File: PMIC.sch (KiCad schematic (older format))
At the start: 37 parts, among them J6 USB_B_Micro, U4 STPMIC1APQR

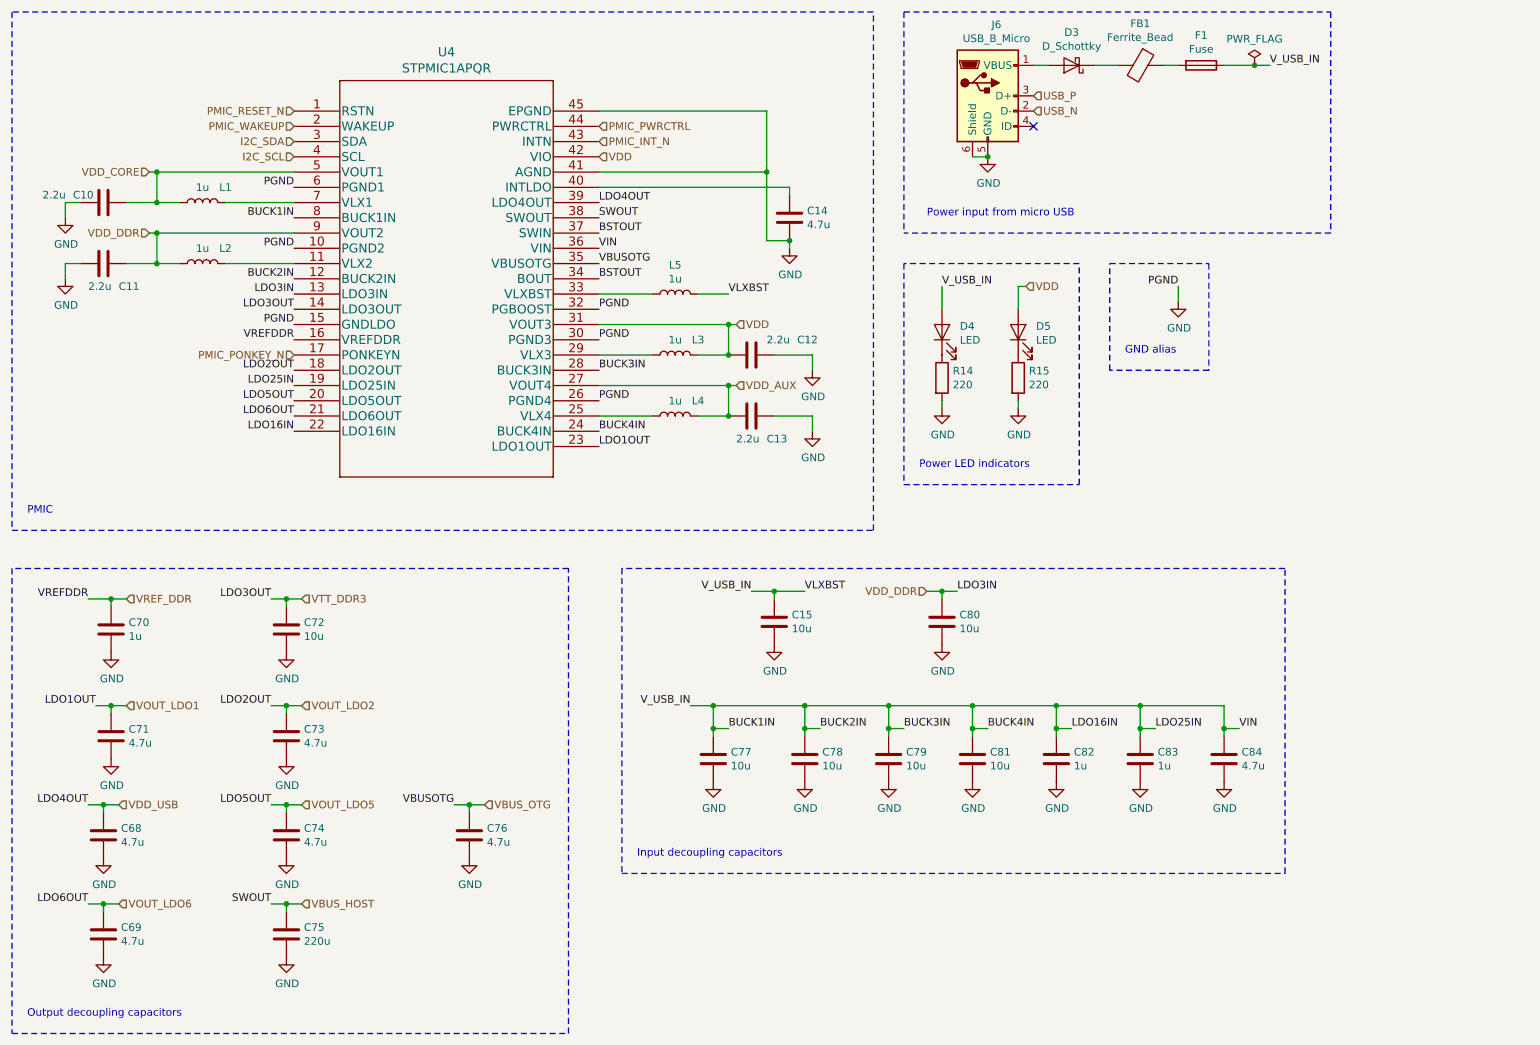
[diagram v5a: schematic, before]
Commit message: Add DC barrel connector for alternate power supply
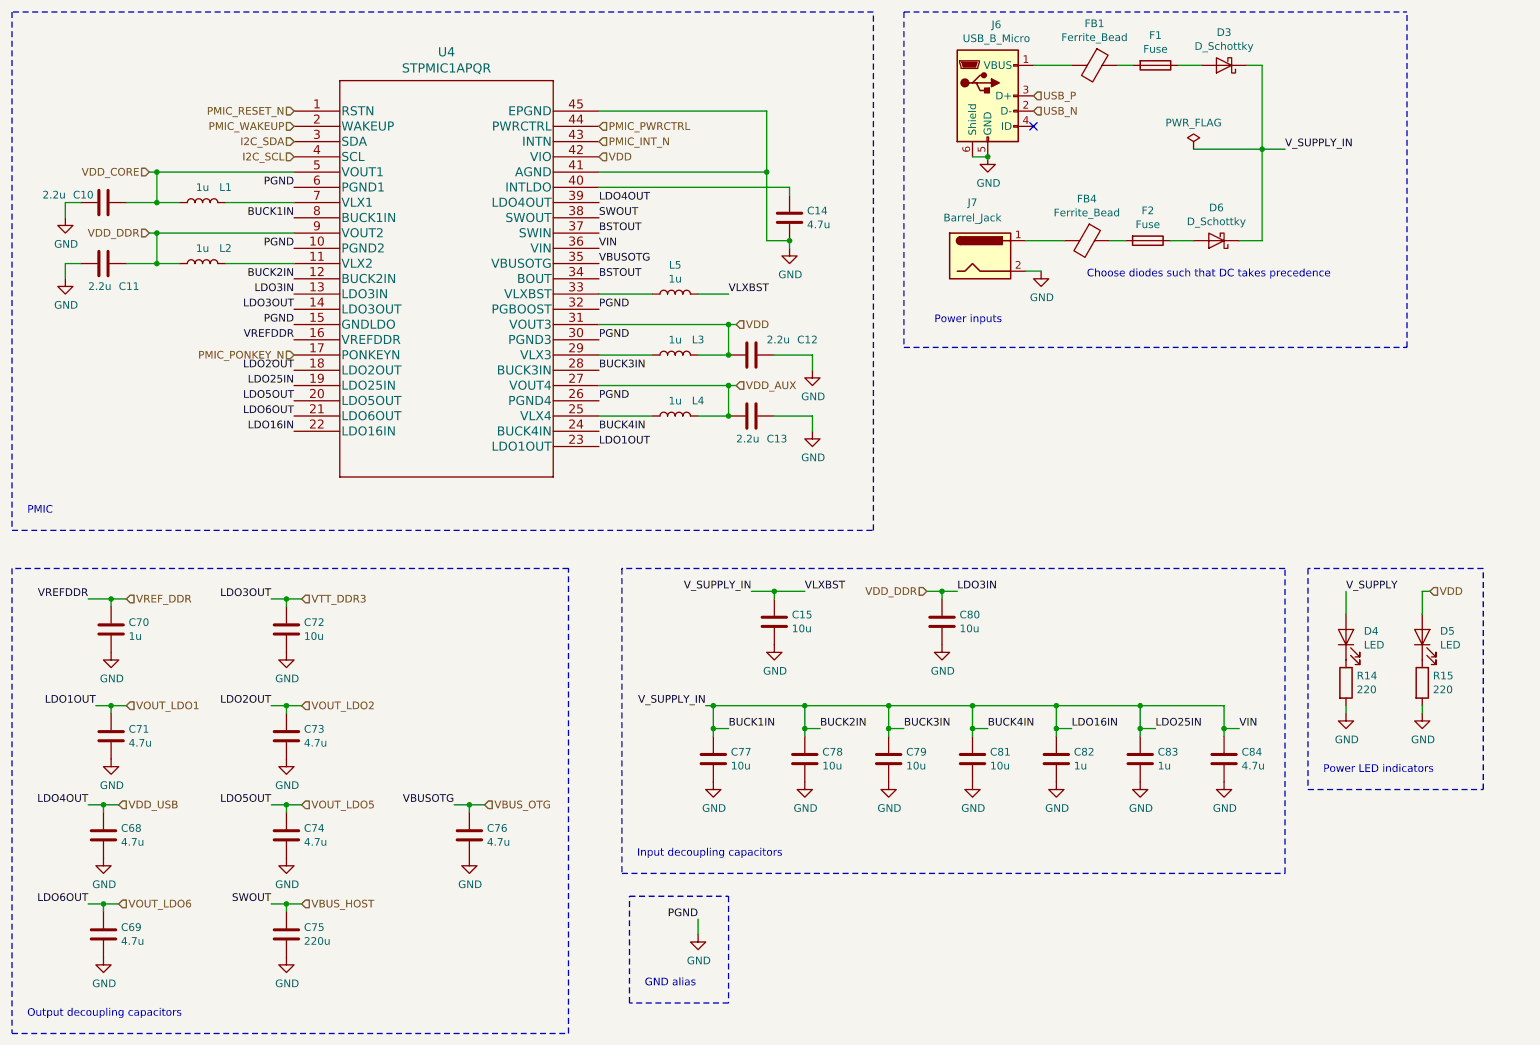
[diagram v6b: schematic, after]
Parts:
- added D6: D_Schottky, Diode_SMD:D_0603_1608Metric, symbol Device:D_Schottky
- added F2: Fuse, Fuse:Fuse_0603_1608Metric, symbol Device:Fuse
- added FB4: Ferrite_Bead, Inductor_SMD:L_0603_1608Metric, symbol Device:Ferrite_Bead
- added J7: Barrel_Jack, symbol Connector:Barrel_Jack
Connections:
- net BUCK1IN: now also D3.1 (K), D6.1 (K); no longer D4.2 (A), F1.1
- net GND: now also J7.2
- net at J6.1 (VBUS): now also FB1.2; no longer D3.2 (A)
- new net: D3.2 (A), F1.1
- new net: FB4.2, J7.1
- new net: D6.2 (A), F2.1
- new net: F2.2, FB4.1
- new net V_SUPPLY: D4.2 (A)
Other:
- note added: "Choose diodes such that DC takes precedence"
- note added: "Power inputs"
- note removed: "Power input from micro USB"
- moved on the sheet: D3, D4, D5, F1, FB1, R14, R15

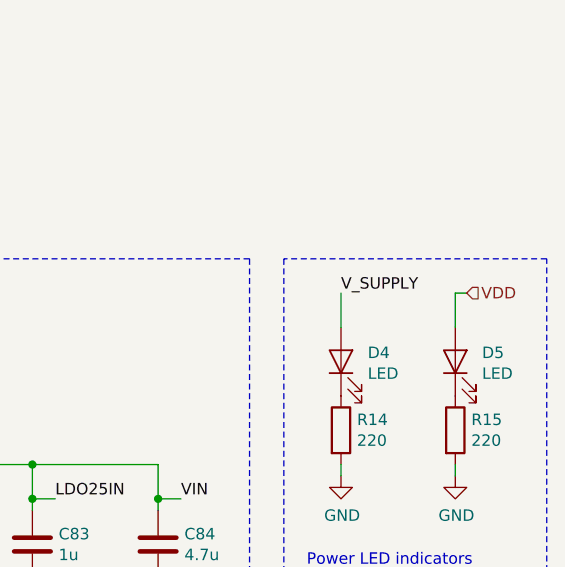
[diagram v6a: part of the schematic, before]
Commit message: Start crossing off ERC. Add generated BOM
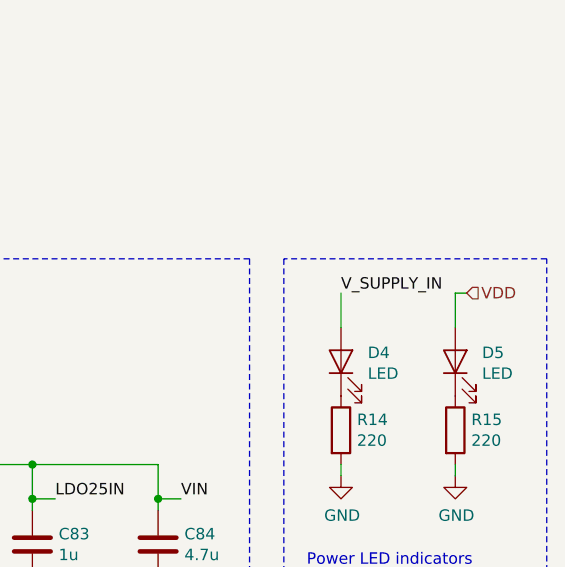
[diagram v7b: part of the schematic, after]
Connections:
- net V_SUPPLY is gone; now on net BUCK1IN: D4.2 (A)
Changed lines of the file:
@@
 $Descr A4 11693 8268
 encoding utf-8
-Sheet 6 6
+Sheet 5 6
 Title ""
 Date ""
@@
 Connection ~ 7500 1700
 Text Label 9850 4550 0    50   ~ 0
-V_SUPPLY
+V_SUPPLY_IN
 $Comp
 L Device:R R14
@@
 Wire Wire Line
 	6100 3400 6350 3400
-Wire Wire Line
-	6100 3000 6350 3000
 Wire Wire Line
 	5850 3200 5800 3200
@@
 Wire Notes Line
 	6950 750  6950 2950
+Wire Wire Line
+	6100 3000 6350 3000
 $EndSCHEMATC

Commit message: Complete schematic rough draft
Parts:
- added R34, R35: 0, symbol Device:R
- added SW5: SW_Push, symbol Switch:SW_Push
- added TP1: TestPoint, symbol Connector:TestPoint
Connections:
- net BUCK1IN: now also TP1.1
- net GND: now also SW5.2
- net VBUS_HOST: now also R34.1; no longer C75.1, U4.38 (SWOUT)
- net VBUS_OTG: now also R35.1
- net at FB1.2, J6.1 (VBUS): now also R35.2
- net PMIC_PONKEY_N renamed PONKEY_N
- net PONKEY_N: now also SW5.1
- new net SWOUT: C75.1, R34.2, U4.38 (SWOUT)
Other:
- note added: "Reset Button\n"
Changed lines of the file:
@@
 	-1   0    0    1
-$EndComp
-$Comp
-L Device:Ferrite_Bead FB?
-U 1 1 60637B8B
-P 8200 1100
-AR Path="/601728C0/60637B8B" Ref="FB?"  Part="1"
-AR Path="/60172B24/60637B8B" Ref="FB1"  Part="1"
-F 0 "FB1" V 7926 1100 50  0000 C CNN
-F 1 "Ferrite_Bead" V 8017 1100 50  0000 C CNN
-F 2 "Inductor_SMD:L_0603_1608Metric" V 8130 1100 50  0001 C CNN
-F 3 "~" H 8200 1100 50  0001 C CNN
-	1    8200 1100
-	0    1    1    0
 $EndComp
 Wire Wire Line
@@
 Wire Wire Line
 	9850 5350 9850 5300
-Text Label 5600 6700 2    50   ~ 0
+Text Label 5550 6700 2    50   ~ 0
 PGND
 Text Label 2950 1900 2    50   ~ 0
@@
 Wire Wire Line
 	2050 2000 2050 1800
-Wire Wire Line
-	2050 1800 2950 1800
 $Comp
 L Device:L L2
@@
 Wire Wire Line
 	4950 3400 5300 3400
-Text HLabel 3000 6600 2    50   Input ~ 0
+Text HLabel 3450 6600 2    50   Input ~ 0
 VBUS_HOST
 Text HLabel 3000 4600 2    50   Input ~ 0
@@
 Text HLabel 1850 4600 2    50   Input ~ 0
 VREF_DDR
-Text HLabel 3000 5300 2    50   Input ~ 0
-VOUT_LDO2
 Text HLabel 1850 5300 2    50   Input ~ 0
 VOUT_LDO1
@@
 Text Label 2950 2800 2    50   ~ 0
 PGND
-Text HLabel 2950 3000 0    50   Input ~ 0
-PMIC_PONKEY_N
 Text HLabel 2950 1400 0    50   Input ~ 0
 PMIC_RESET_N
@@
 	1    0    0    -1
 $EndComp
-Text Label 2800 5300 2    50   ~ 0
-LDO2OUT
-$Comp
-L Device:C C73
-U 1 1 6173BB67
-P 2900 5500
-F 0 "C73" H 3015 5546 50  0000 L CNN
-F 1 "4.7u" H 3015 5455 50  0000 L CNN
-F 2 "" H 2938 5350 50  0001 C CNN
-F 3 "~" H 2900 5500 50  0001 C CNN
-	1    2900 5500
-	1    0    0    -1
-$EndComp
-Wire Wire Line
-	2900 5350 2900 5300
-Wire Wire Line
-	2900 5300 2800 5300
-Wire Wire Line
-	2900 5300 3000 5300
-Connection ~ 2900 5300
-$Comp
-L power:GND #PWR0116
-U 1 1 6173BB71
-P 2900 5650
-F 0 "#PWR0116" H 2900 5400 50  0001 C CNN
-F 1 "GND" H 2905 5477 50  0000 C CNN
-F 2 "" H 2900 5650 50  0001 C CNN
-F 3 "" H 2900 5650 50  0001 C CNN
-	1    2900 5650
-	1    0    0    -1
-$EndComp
 Text Label 1600 5950 2    50   ~ 0
 LDO4OUT
@@
 Wire Wire Line
 	2900 6600 2800 6600
-Wire Wire Line
-	2900 6600 3000 6600
 Connection ~ 2900 6600
 $Comp
@@
 Text Label 4950 2400 0    50   ~ 0
 VBUSOTG
-Text Label 4000 5950 2    50   ~ 0
-VBUSOTG
-Text HLabel 4200 5950 2    50   Input ~ 0
-VBUS_OTG
-$Comp
-L Device:C C76
-U 1 1 618A2F29
-P 4100 6150
-F 0 "C76" H 4215 6196 50  0000 L CNN
-F 1 "4.7u" H 4215 6105 50  0000 L CNN
-F 2 "" H 4138 6000 50  0001 C CNN
-F 3 "~" H 4100 6150 50  0001 C CNN
-	1    4100 6150
-	1    0    0    -1
-$EndComp
-Wire Wire Line
-	4100 6000 4100 5950
-Wire Wire Line
-	4100 5950 4000 5950
-Wire Wire Line
-	4100 5950 4200 5950
-Connection ~ 4100 5950
-$Comp
-L power:GND #PWR0127
-U 1 1 618A2F33
-P 4100 6300
-F 0 "#PWR0127" H 4100 6050 50  0001 C CNN
-F 1 "GND" H 4105 6127 50  0000 C CNN
-F 2 "" H 4100 6300 50  0001 C CNN
-F 3 "" H 4100 6300 50  0001 C CNN
-	1    4100 6300
-	1    0    0    -1
-$EndComp
 Text Notes 1200 7350 0    50   ~ 0
 Output decoupling capacitors
@@
 L power:GND #PWR029
 U 1 1 60FFDCB0
-P 5600 6800
-F 0 "#PWR029" H 5600 6550 50  0001 C CNN
-F 1 "GND" H 5605 6627 50  0000 C CNN
-F 2 "" H 5600 6800 50  0001 C CNN
-F 3 "" H 5600 6800 50  0001 C CNN
-	1    5600 6800
-	1    0    0    -1
-$EndComp
-Wire Wire Line
-	5600 6800 5600 6700
+P 5550 6800
+F 0 "#PWR029" H 5550 6550 50  0001 C CNN
+F 1 "GND" H 5555 6627 50  0000 C CNN
+F 2 "" H 5550 6800 50  0001 C CNN
+F 3 "" H 5550 6800 50  0001 C CNN
+	1    5550 6800
+	1    0    0    -1
+$EndComp
+Wire Wire Line
+	5550 6800 5550 6700
 Text Notes 7150 2800 0    50   ~ 0
 Power inputs
@@
 Text Notes 9700 5750 0    50   ~ 0
 Power LED indicators
-Text Notes 5250 7150 0    50   ~ 0
+Text Notes 5200 7150 0    50   ~ 0
 GND alias\n
 Wire Notes Line
@@
 	1100 4400 1100 7450
 Wire Notes Line
-	5150 7250 5150 6550
-Wire Notes Line
-	5150 6550 5800 6550
-Wire Notes Line
-	5800 6550 5800 7250
-Wire Notes Line
-	5800 7250 5150 7250
+	5100 7250 5100 6550
+Wire Notes Line
+	5100 6550 5750 6550
+Wire Notes Line
+	5750 6550 5750 7250
+Wire Notes Line
+	5750 7250 5100 7250
 Wire Notes Line
 	9450 6400 9450 4400
@@
 Wire Notes Line
 	1100 750  1100 4150
-Text HLabel 7800 1300 2    50   Input ~ 0
+Text HLabel 8050 1300 2    50   Input ~ 0
 USB_P
-Text HLabel 7800 1400 2    50   Input ~ 0
+Text HLabel 8050 1400 2    50   Input ~ 0
 USB_N
 $Comp
@@
 	7750 2250 8000 2250
 Wire Wire Line
-	7800 1100 8050 1100
-Wire Wire Line
 	8850 2250 8700 2250
 Wire Wire Line
@@
 Wire Wire Line
 	9300 1650 9300 1100
+Text Notes 8150 2500 0    50   ~ 0
+Choose diodes such that DC takes precedence
+Wire Notes Line
+	6950 2950 10250 2950
+Wire Notes Line
+	10250 2950 10250 750
+Wire Notes Line
+	6950 750  10250 750
+Wire Notes Line
+	6950 750  6950 2950
+Wire Wire Line
+	6100 3000 6350 3000
+$Comp
+L Device:R R34
+U 1 1 60E1534B
+P 3150 6600
+F 0 "R34" V 2943 6600 50  0000 C CNN
+F 1 "0" V 3034 6600 50  0000 C CNN
+F 2 "" V 3080 6600 50  0001 C CNN
+F 3 "~" H 3150 6600 50  0001 C CNN
+	1    3150 6600
+	0    1    1    0
+$EndComp
+Wire Wire Line
+	2900 6600 3000 6600
+$Comp
+L power:GND #PWR0116
+U 1 1 6173BB71
+P 2900 5650
+F 0 "#PWR0116" H 2900 5400 50  0001 C CNN
+F 1 "GND" H 2905 5477 50  0000 C CNN
+F 2 "" H 2900 5650 50  0001 C CNN
+F 3 "" H 2900 5650 50  0001 C CNN
+	1    2900 5650
+	1    0    0    -1
+$EndComp
+Connection ~ 2900 5300
+Wire Wire Line
+	2900 5300 3000 5300
+Wire Wire Line
+	2900 5300 2800 5300
+Wire Wire Line
+	2900 5350 2900 5300
+$Comp
+L Device:C C73
+U 1 1 6173BB67
+P 2900 5500
+F 0 "C73" H 3015 5546 50  0000 L CNN
+F 1 "4.7u" H 3015 5455 50  0000 L CNN
+F 2 "" H 2938 5350 50  0001 C CNN
+F 3 "~" H 2900 5500 50  0001 C CNN
+	1    2900 5500
+	1    0    0    -1
+$EndComp
+Text Label 2800 5300 2    50   ~ 0
+LDO2OUT
+Text HLabel 3000 5300 2    50   Input ~ 0
+VOUT_LDO2
+$Comp
+L power:GND #PWR0127
+U 1 1 618A2F33
+P 4100 6300
+F 0 "#PWR0127" H 4100 6050 50  0001 C CNN
+F 1 "GND" H 4105 6127 50  0000 C CNN
+F 2 "" H 4100 6300 50  0001 C CNN
+F 3 "" H 4100 6300 50  0001 C CNN
+	1    4100 6300
+	1    0    0    -1
+$EndComp
+Connection ~ 4100 5950
+Wire Wire Line
+	4100 5950 4200 5950
+Wire Wire Line
+	4100 5950 4000 5950
+Wire Wire Line
+	4100 6000 4100 5950
+$Comp
+L Device:C C76
+U 1 1 618A2F29
+P 4100 6150
+F 0 "C76" H 4215 6196 50  0000 L CNN
+F 1 "4.7u" H 4215 6105 50  0000 L CNN
+F 2 "" H 4138 6000 50  0001 C CNN
+F 3 "~" H 4100 6150 50  0001 C CNN
+	1    4100 6150
+	1    0    0    -1
+$EndComp
+Text HLabel 4200 5950 2    50   Input ~ 0
+VBUS_OTG
+Text Label 4000 5950 2    50   ~ 0
+VBUSOTG
+$Comp
+L Switch:SW_Push SW?
+U 1 1 60F3BCED
+P 7650 3500
+AR Path="/60172A77/60F3BCED" Ref="SW?"  Part="1"
+AR Path="/60172B24/60F3BCED" Ref="SW5"  Part="1"
+F 0 "SW5" V 7604 3648 50  0000 L CNN
+F 1 "SW_Push" V 7695 3648 50  0000 L CNN
+F 2 "" H 7650 3700 50  0001 C CNN
+F 3 "~" H 7650 3700 50  0001 C CNN
+	1    7650 3500
+	0    1    1    0
+$EndComp
+$Comp
+L power:GND #PWR?
+U 1 1 60F3BCF7
+P 7500 3700
+AR Path="/60172A77/60F3BCF7" Ref="#PWR?"  Part="1"
+AR Path="/60172B24/60F3BCF7" Ref="#PWR035"  Part="1"
+F 0 "#PWR035" H 7500 3450 50  0001 C CNN
+F 1 "GND" H 7505 3527 50  0000 C CNN
+F 2 "" H 7500 3700 50  0001 C CNN
+F 3 "" H 7500 3700 50  0001 C CNN
+	1    7500 3700
+	1    0    0    -1
+$EndComp
+Wire Wire Line
+	7500 3700 7650 3700
+Text Notes 7050 4050 0    50   ~ 0
+Reset Button\n
+Text Label 7650 3300 2    50   ~ 0
+PONKEY_N
+Wire Notes Line
+	6950 3050 6950 4150
+Wire Notes Line
+	6950 4150 8350 4150
+Wire Notes Line
+	8350 4150 8350 3050
+Wire Notes Line
+	8350 3050 6950 3050
+Text Label 2950 3000 2    50   ~ 0
+PONKEY_N
+Wire Wire Line
+	9450 1650 9300 1650
 Text Label 9450 1650 0    50   ~ 0
 V_SUPPLY_IN
-Wire Wire Line
-	9450 1650 9300 1650
-Text Notes 8150 2500 0    50   ~ 0
-Choose diodes such that DC takes precedence
-Wire Notes Line
-	6950 2950 10250 2950
-Wire Notes Line
-	10250 2950 10250 750
-Wire Notes Line
-	6950 750  10250 750
-Wire Notes Line
-	6950 750  6950 2950
-Wire Wire Line
-	6100 3000 6350 3000
+$Comp
+L Device:Ferrite_Bead FB?
+U 1 1 60637B8B
+P 8200 1100
+AR Path="/601728C0/60637B8B" Ref="FB?"  Part="1"
+AR Path="/60172B24/60637B8B" Ref="FB1"  Part="1"
+F 0 "FB1" V 7926 1100 50  0000 C CNN
+F 1 "Ferrite_Bead" V 8017 1100 50  0000 C CNN
+F 2 "Inductor_SMD:L_0603_1608Metric" V 8130 1100 50  0001 C CNN
+F 3 "~" H 8200 1100 50  0001 C CNN
+	1    8200 1100
+	0    1    1    0
+$EndComp
+$Comp
+L Connector:TestPoint TP1
+U 1 1 6101333B
+P 7950 5300
+F 0 "TP1" H 8008 5418 50  0000 L CNN
+F 1 "TestPoint" H 8008 5327 50  0000 L CNN
+F 2 "" H 8150 5300 50  0001 C CNN
+F 3 "~" H 8150 5300 50  0001 C CNN
+	1    7950 5300
+	1    0    0    -1
+$EndComp
+Text Label 8350 1650 0    50   ~ 0
+VBUSOTG
+$Comp
+L Device:R R35
+U 1 1 610A006A
+P 8150 1650
+F 0 "R35" V 8250 1700 50  0000 C CNN
+F 1 "0" V 8250 1600 50  0000 C CNN
+F 2 "" V 8080 1650 50  0001 C CNN
+F 3 "~" H 8150 1650 50  0001 C CNN
+	1    8150 1650
+	0    1    1    0
+$EndComp
+Wire Wire Line
+	8300 1650 8350 1650
+Wire Wire Line
+	8000 1650 7950 1650
+Wire Wire Line
+	7950 1650 7950 1100
+Wire Wire Line
+	7800 1100 7950 1100
+Connection ~ 7950 1100
+Wire Wire Line
+	7950 1100 8050 1100
+Wire Wire Line
+	8050 1400 7800 1400
+Wire Wire Line
+	7800 1300 8050 1300
+Wire Wire Line
+	2050 1800 2950 1800
+Wire Wire Line
+	3300 6600 3350 6600
+$Comp
+L power:PWR_FLAG #FLG0103
+U 1 1 611C8FCC
+P 3500 6500
+F 0 "#FLG0103" H 3500 6575 50  0001 C CNN
+F 1 "PWR_FLAG" H 3500 6673 50  0000 C CNN
+F 2 "" H 3500 6500 50  0001 C CNN
+F 3 "~" H 3500 6500 50  0001 C CNN
+	1    3500 6500
+	1    0    0    -1
+$EndComp
+Wire Wire Line
+	3500 6500 3350 6500
+Wire Wire Line
+	3350 6500 3350 6600
+Connection ~ 3350 6600
+Wire Wire Line
+	3350 6600 3450 6600
 $EndSCHEMATC
